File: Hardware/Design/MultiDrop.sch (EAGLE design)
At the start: 14 parts

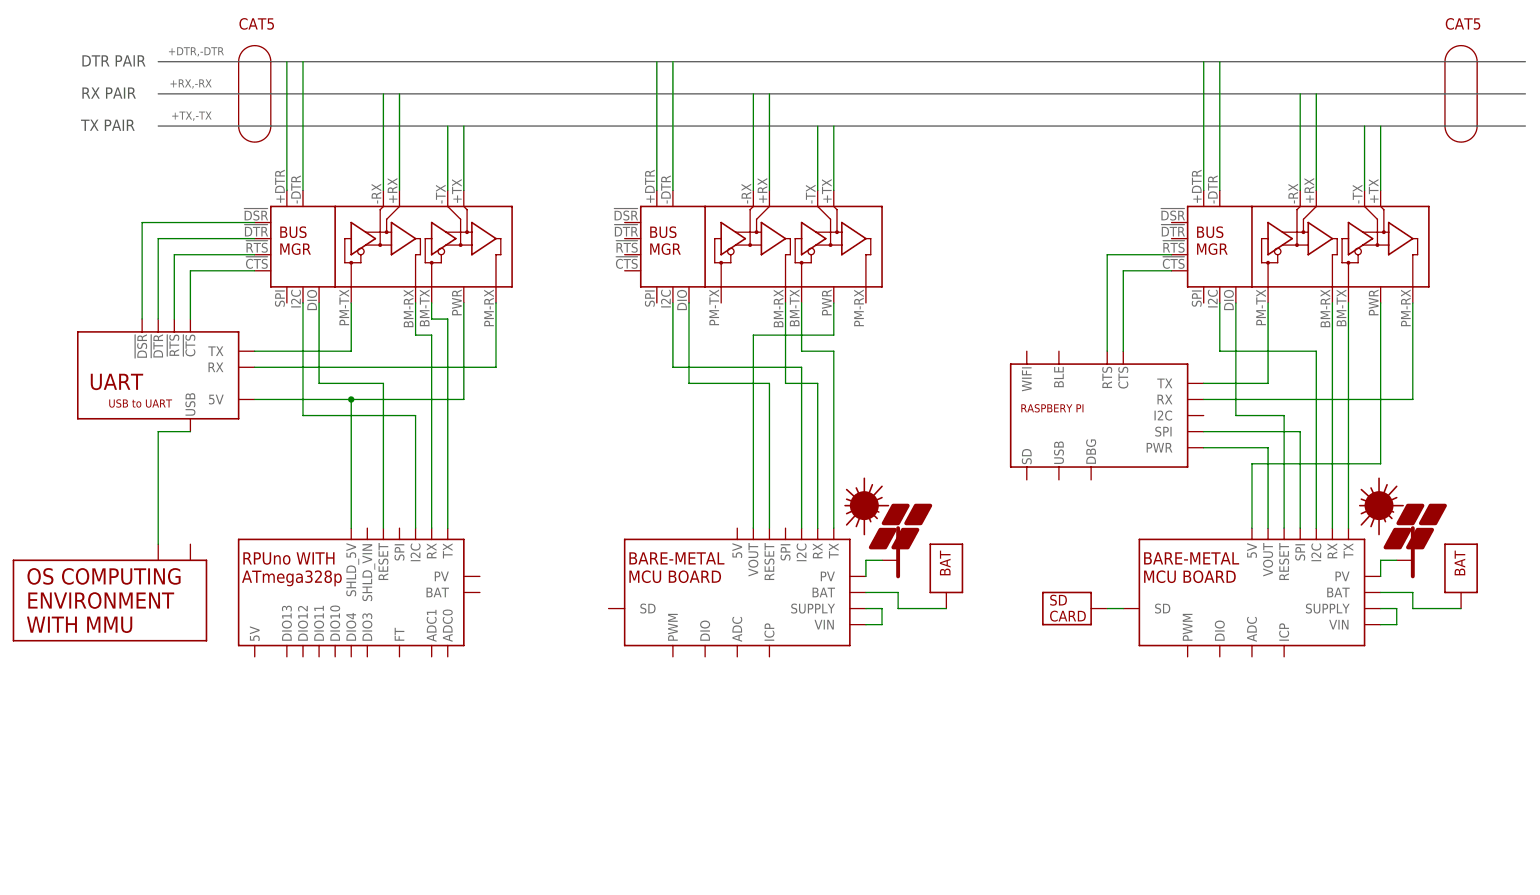
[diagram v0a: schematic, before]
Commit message: example is a little more refined
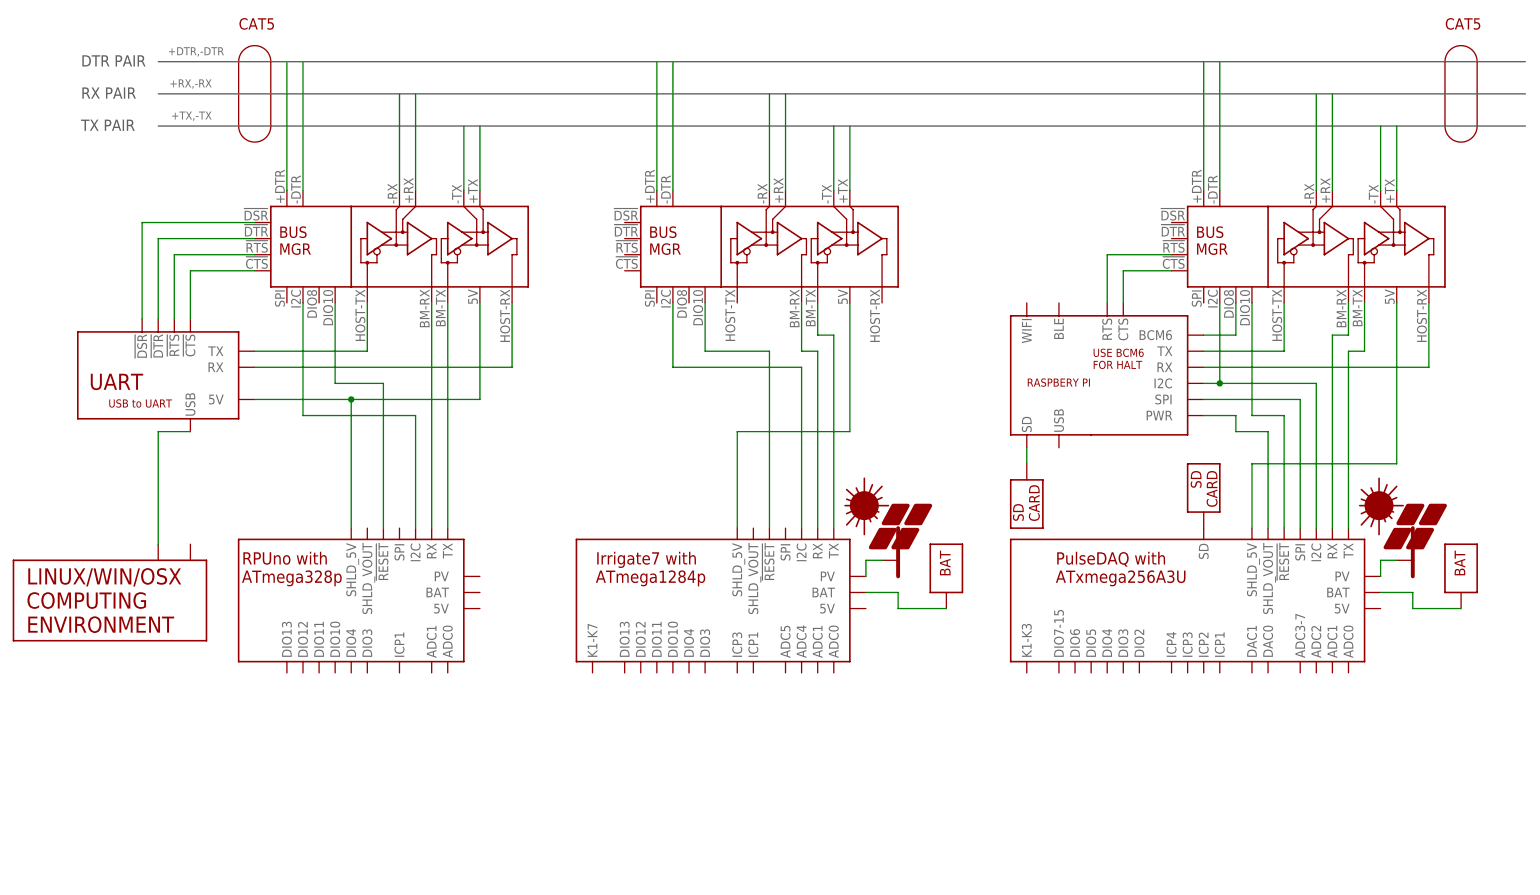
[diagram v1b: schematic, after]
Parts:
- removed BM1, BM3: (no value), Documentation:BARE-METAL
- removed PM2: (no value), Documentation:TRUSTWORTHY
- added PM1: (no value), Documentation:DESKTOP
- added SD2: SD, Documentation:SD
- added U$4: BUS_MGR, Documentation:BUS_MGR
- added U$6: PULSEDAQ, Documentation:PULSEDAQ
- U$5: value BUS_MGR -> IRRIGATE7; device Documentation:BUS_MGR -> Documentation:IRRIGATE7
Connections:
- removed net N$38: BM1.SUPPLY, BM1.VIN
- removed net N$40: BM3.SUPPLY, BM3.VIN
- removed net N$42: BM3.SD, SD3.PV_PWR
- new net N$13: U$1.PWR, U$6.SHLD_5V
- new net N$16: SD3.PV_PWR, U$6.SD
- new net N$28: SD2.PV_PWR, U$3.SD
- net +DTR: now also U$4.+DTR; no longer U$1.+DTR
- net +DTR3: now also U$1.+DTR; no longer U$5.+DTR
- net +RX: now also U$4.+RX; no longer U$1.+RX
- net +RX3: now also U$1.+RX; no longer U$5.+RX
- net +TX: now also U$4.+TX; no longer U$1.+TX
- net +TX3: now also U$1.+TX; no longer U$5.+TX
- net -DTR: now also U$4.-DTR; no longer U$1.-DTR
- net -DTR3: now also U$1.-DTR; no longer U$5.-DTR
- net -RX: now also U$4.-RX; no longer U$1.-RX
- net -RX3: now also U$1.-RX; no longer U$5.-RX
- net -TX: now also U$4.-TX; no longer U$1.-TX
- net -TX3: now also U$1.-TX; no longer U$5.-TX
- net N$1: now also U$4.BM_TX; no longer U$1.BM_TX
- net N$10: now also U$5.TX; no longer BM1.TX
- net N$11: now also U$5.RX; no longer BM1.RX
- net N$12: now also U$1.DIO8, U$3.BCM6; no longer BM3.5V, U$5.PWR
- net N$14: now also U$1.BM_TX, U$6.TX; no longer BM3.TX, U$5.BM_TX
- net N$17: now also U$5.BAT; no longer BM1.BAT
- net N$2: now also U$4.BM_RX; no longer U$1.BM_RX
- net N$21: now also U$1.BM_RX, U$6.RX; no longer BM3.RX, U$5.BM_RX
- net N$22: now also U$1.!CTS; no longer U$5.!CTS
- net N$23: now also U$1.!RTS; no longer U$5.!RTS
- net N$25: now also U$6.SPI; no longer BM3.SPI
- net N$26: now also U$1.HOST_RX; no longer U$5.PM_RX
- net N$27: now also U$1.HOST_TX; no longer U$5.PM_TX
- net N$29: now also U$4.PWR; no longer U$1.PWR
- net N$3: now also PM1.RX; no longer PM2.RX
- net N$30: now also BM2.!RESET, U$4.DIO10; no longer BM2.RESET, U$1.DIO
- net N$31: now also U$6.BAT; no longer BM3.BAT
- net N$32: now also U$1.I2C, U$3.I2C, U$6.I2C; no longer BM3.I2C, U$5.I2C
- net N$33: now also U$4.I2C; no longer U$1.I2C
- net N$34: now also U$6.PV; no longer BM3.PV
- net N$36: now also U$5.PV; no longer BM1.PV
- net N$4: now also U$4.!CTS; no longer U$1.!CTS
- net N$41: now also U$6.SHLD_VOUT; no longer BM3.VOUT
- net N$43: now also U$1.DIO10, U$6.!RESET; no longer BM3.RESET, U$5.DIO
- net N$44: now also U$2.DIO10, U$5.!RESET; no longer BM1.RESET, U$2.DIO
- net N$45: now also U$5.SHLD_5V; no longer BM1.VOUT
- net N$48: now also U$5.I2C; no longer BM1.I2C
- net N$5: now also U$4.!RTS; no longer U$1.!RTS
- net N$6: now also U$4.!DTR; no longer U$1.!DTR
- net N$7: now also U$4.!DSR; no longer U$1.!DSR
- net N$8: now also U$4.HOST_RX; no longer U$1.PM_RX
- net N$9: now also U$4.HOST_TX; no longer U$1.PM_TX
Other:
- note removed: "Irrigate7"
- note removed: "PulseDAQ"
- note removed: "RPUno"

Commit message: Hardware: example
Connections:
- net N$32: no longer U$3.I2C
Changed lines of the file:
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@@
 <wire x1="238.76" y1="93.98" x2="238.76" y2="104.14" width="0.1524" layer="94"/>
 <text x="233.68" y="109.22" size="1.778" layer="94">CAT5</text>
-<text x="165.354" y="82.296" size="5.08" layer="98">RPUpi</text>
+<text x="165.354" y="79.756" size="5.08" layer="98">RPUpi</text>
 <wire x1="15.24" y1="88.9" x2="88.9" y2="88.9" width="0.3048" layer="98" style="shortdash"/>
 <wire x1="88.9" y1="88.9" x2="88.9" y2="43.18" width="0.3048" layer="98" style="shortdash"/>
 <wire x1="88.9" y1="43.18" x2="15.24" y2="43.18" width="0.3048" layer="98" style="shortdash"/>
 <wire x1="15.24" y1="43.18" x2="15.24" y2="88.9" width="0.3048" layer="98" style="shortdash"/>
-<wire x1="93.98" y1="88.9" x2="147.32" y2="88.9" width="0.3048" layer="98" style="shortdash"/>
-<wire x1="147.32" y1="88.9" x2="147.32" y2="43.18" width="0.3048" layer="98" style="shortdash"/>
-<wire x1="147.32" y1="43.18" x2="93.98" y2="43.18" width="0.3048" layer="98" style="shortdash"/>
+<wire x1="93.98" y1="88.9" x2="149.86" y2="88.9" width="0.3048" layer="98" style="shortdash"/>
+<wire x1="149.86" y1="88.9" x2="149.86" y2="43.18" width="0.3048" layer="98" style="shortdash"/>
+<wire x1="149.86" y1="43.18" x2="93.98" y2="43.18" width="0.3048" layer="98" style="shortdash"/>
 <wire x1="93.98" y1="43.18" x2="93.98" y2="88.9" width="0.3048" layer="98" style="shortdash"/>
-<wire x1="157.48" y1="88.9" x2="157.48" y2="43.18" width="0.3048" layer="98" style="shortdash"/>
-<wire x1="157.48" y1="43.18" x2="238.76" y2="43.18" width="0.3048" layer="98" style="shortdash"/>
+<wire x1="157.48" y1="88.9" x2="157.48" y2="66.04" width="0.3048" layer="98" style="shortdash"/>
+<wire x1="157.48" y1="66.04" x2="190.5" y2="66.04" width="0.3048" layer="98" style="shortdash"/>
+<wire x1="190.5" y1="66.04" x2="190.5" y2="43.18" width="0.3048" layer="98" style="shortdash"/>
+<wire x1="190.5" y1="43.18" x2="238.76" y2="43.18" width="0.3048" layer="98" style="shortdash"/>
 <wire x1="238.76" y1="43.18" x2="238.76" y2="88.9" width="0.3048" layer="98" style="shortdash"/>
 <wire x1="238.76" y1="88.9" x2="157.48" y2="88.9" width="0.3048" layer="98" style="shortdash"/>
@@
 <instance part="PV2" gate="G$1" x="147.32" y="25.4"/>
 <instance part="PV4" gate="G$1" x="228.6" y="25.4"/>
-<instance part="SD2" gate="G$1" x="167.64" y="33.02" rot="R90"/>
+<instance part="SD2" gate="G$1" x="162.56" y="35.56" rot="R90"/>
 <instance part="U$7" gate="G$1" x="236.22" y="25.4" rot="R270"/>
 <instance part="U$9" gate="G$1" x="154.94" y="25.4" rot="R270"/>
-<instance part="SD3" gate="G$1" x="195.58" y="38.1" rot="R270"/>
+<instance part="SD3" gate="G$1" x="172.72" y="38.1" rot="R270"/>
 <instance part="BM2" gate="G$1" x="60.96" y="20.32"/>
-<instance part="U$3" gate="G$1" x="175.26" y="55.88"/>
+<instance part="U$3" gate="G$1" x="170.18" y="55.88"/>
 <instance part="U$1" gate="G$1" x="215.9" y="76.2"/>
 <instance part="U$2" gate="G$1" x="129.54" y="76.2"/>
@@
 <net name="N$22" class="0">
 <segment>
-<wire x1="190.5" y1="71.12" x2="182.88" y2="71.12" width="0.1524" layer="91"/>
-<wire x1="182.88" y1="71.12" x2="182.88" y2="66.04" width="0.1524" layer="91"/>
+<wire x1="190.5" y1="71.12" x2="177.8" y2="71.12" width="0.1524" layer="91"/>
+<wire x1="177.8" y1="71.12" x2="177.8" y2="66.04" width="0.1524" layer="91"/>
 <pinref part="U$3" gate="G$1" pin="CTS"/>
 <pinref part="U$1" gate="G$1" pin="!CTS"/>
@@
 <net name="N$23" class="0">
 <segment>
-<wire x1="180.34" y1="66.04" x2="180.34" y2="73.66" width="0.1524" layer="91"/>
-<wire x1="180.34" y1="73.66" x2="190.5" y2="73.66" width="0.1524" layer="91"/>
+<wire x1="175.26" y1="66.04" x2="175.26" y2="73.66" width="0.1524" layer="91"/>
+<wire x1="175.26" y1="73.66" x2="190.5" y2="73.66" width="0.1524" layer="91"/>
 <pinref part="U$3" gate="G$1" pin="RTS"/>
 <pinref part="U$1" gate="G$1" pin="!RTS"/>
@@
 <segment>
 <wire x1="231.14" y1="55.88" x2="231.14" y2="66.04" width="0.1524" layer="91"/>
-<wire x1="195.58" y1="55.88" x2="231.14" y2="55.88" width="0.1524" layer="91"/>
+<wire x1="190.5" y1="55.88" x2="231.14" y2="55.88" width="0.1524" layer="91"/>
 <pinref part="U$3" gate="G$1" pin="RX"/>
 <pinref part="U$1" gate="G$1" pin="HOST_RX"/>
@@
 <segment>
 <wire x1="208.28" y1="58.42" x2="208.28" y2="66.04" width="0.1524" layer="91"/>
-<wire x1="195.58" y1="58.42" x2="208.28" y2="58.42" width="0.1524" layer="91"/>
+<wire x1="190.5" y1="58.42" x2="208.28" y2="58.42" width="0.1524" layer="91"/>
 <pinref part="U$3" gate="G$1" pin="TX"/>
 <pinref part="U$1" gate="G$1" pin="HOST_TX"/>
@@
 <wire x1="213.36" y1="53.34" x2="198.12" y2="53.34" width="0.1524" layer="91"/>
 <wire x1="198.12" y1="53.34" x2="198.12" y2="66.04" width="0.1524" layer="91"/>
-<wire x1="195.58" y1="53.34" x2="198.12" y2="53.34" width="0.1524" layer="91"/>
-<junction x="198.12" y="53.34"/>
-<pinref part="U$3" gate="G$1" pin="I2C"/>
 <pinref part="U$1" gate="G$1" pin="I2C"/>
 <pinref part="U$6" gate="G$1" pin="I2C"/>
@@
 <net name="N$25" class="0">
 <segment>
-<wire x1="195.58" y1="50.8" x2="210.82" y2="50.8" width="0.1524" layer="91"/>
+<wire x1="190.5" y1="50.8" x2="210.82" y2="50.8" width="0.1524" layer="91"/>
 <wire x1="210.82" y1="50.8" x2="210.82" y2="30.48" width="0.1524" layer="91"/>
 <pinref part="U$3" gate="G$1" pin="SPI"/>
@@
 <pinref part="SD2" gate="G$1" pin="PV_PWR"/>
 <pinref part="U$3" gate="G$1" pin="SD"/>
-<wire x1="167.64" y1="40.64" x2="167.64" y2="43.18" width="0.1524" layer="91"/>
 </segment>
 </net>
@@
 <pinref part="U$3" gate="G$1" pin="PWR"/>
 <pinref part="U$6" gate="G$1" pin="SHLD_VOUT"/>
-<wire x1="200.66" y1="48.26" x2="195.58" y2="48.26" width="0.1524" layer="91"/>
+<wire x1="190.5" y1="48.26" x2="200.66" y2="48.26" width="0.1524" layer="91"/>
 <wire x1="200.66" y1="48.26" x2="200.66" y2="45.72" width="0.1524" layer="91"/>
 <wire x1="200.66" y1="45.72" x2="205.74" y2="45.72" width="0.1524" layer="91"/>
@@
 <segment>
 <pinref part="U$3" gate="G$1" pin="BCM6"/>
-<wire x1="195.58" y1="60.96" x2="200.66" y2="60.96" width="0.1524" layer="91"/>
+<wire x1="190.5" y1="60.96" x2="200.66" y2="60.96" width="0.1524" layer="91"/>
 <pinref part="U$1" gate="G$1" pin="DIO8"/>
 <wire x1="200.66" y1="60.96" x2="200.66" y2="66.04" width="0.1524" layer="91"/>

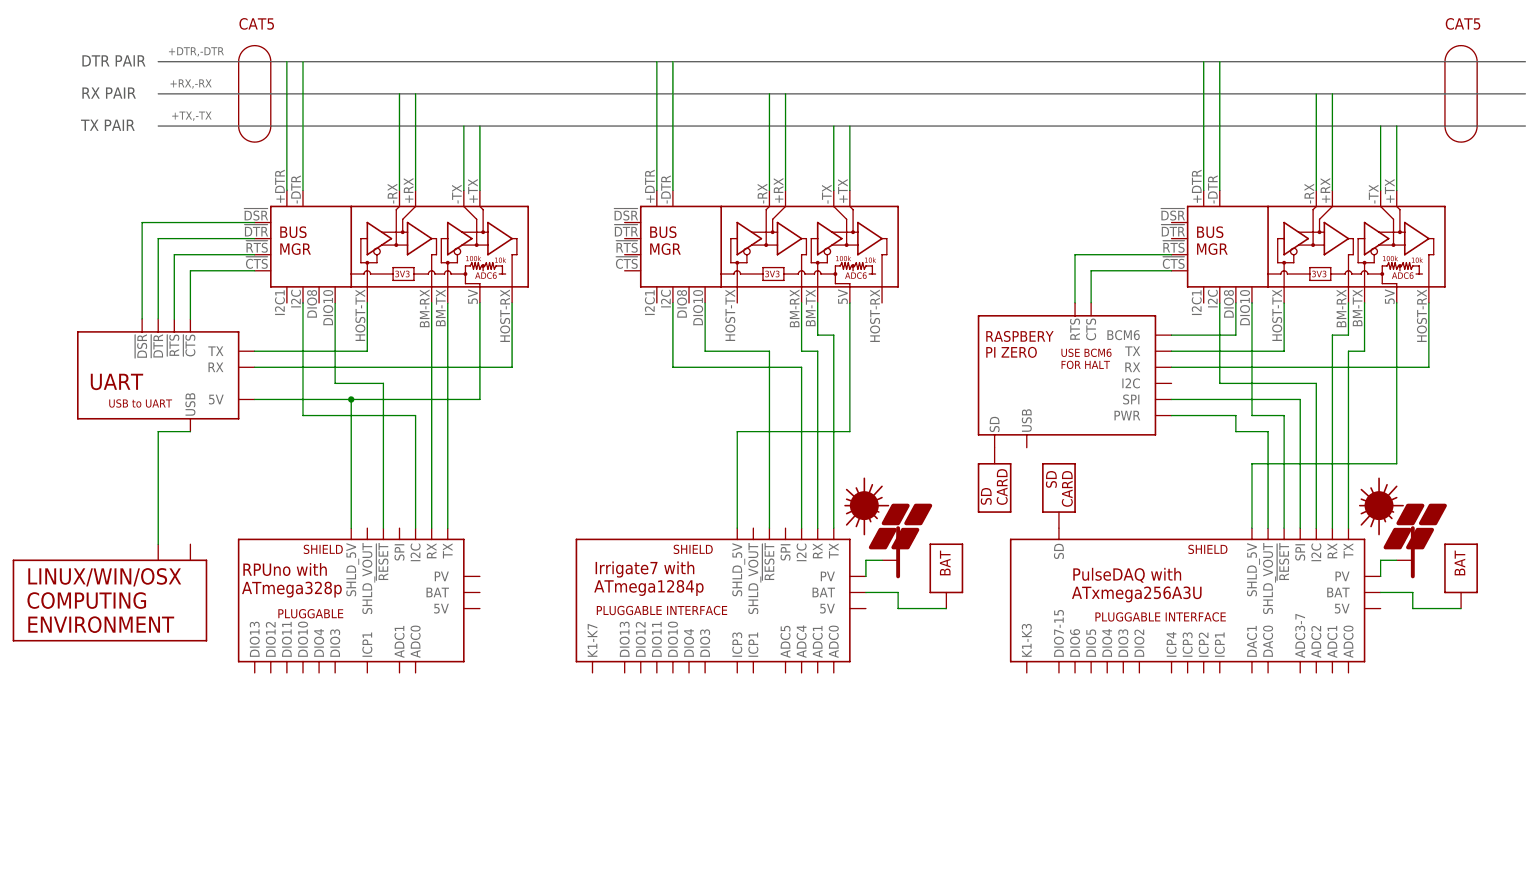
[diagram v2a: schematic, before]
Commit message: Hardware: update multidrop example
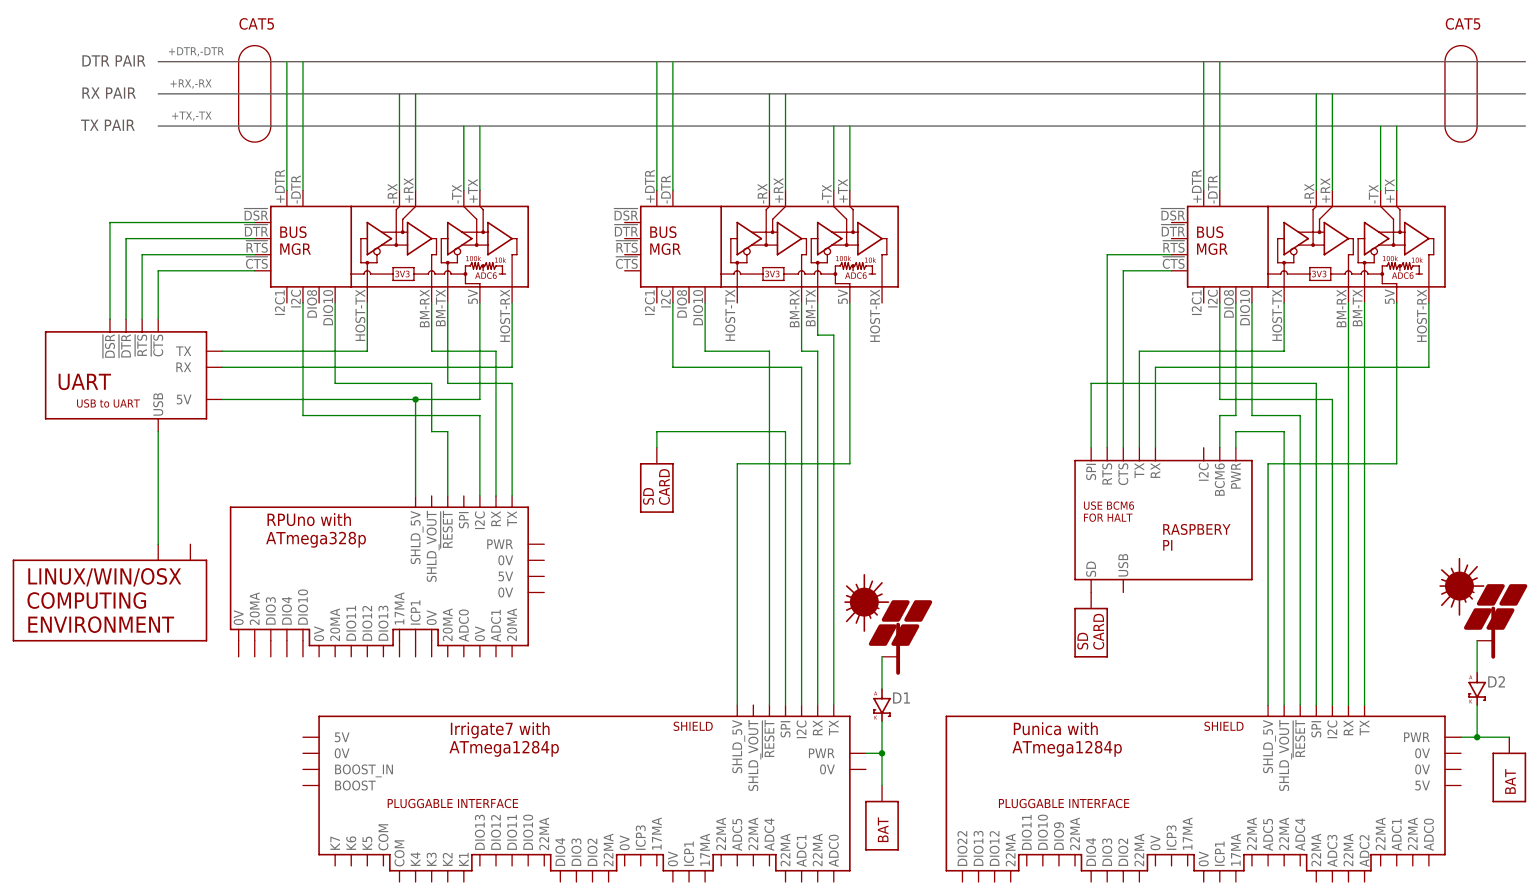
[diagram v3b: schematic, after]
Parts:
- removed SD3: SD, Documentation:SD
- removed U$6: PULSEDAQ, Documentation:PULSEDAQ
- added D1, D2: (no value), D-SBR:DSMB
- added SD1: SD, Documentation:SD
- added U$8: PUNICA, Documentation:PUNICA
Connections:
- removed net N$31: U$6.BAT, U$7.BAT_PWR
- removed net N$34: PV4.PV_PWR, U$6.PV
- removed net N$36: PV2.PV_PWR, U$5.PV
- new net N$15: D2.K, U$7.BAT_PWR, U$8.PWR
- new net N$18: D1.K, U$5.PWR, U$9.BAT_PWR
- new net N$19: SD1.PV_PWR, U$5.SPI
- net N$13: now also U$8.SHLD_5V; no longer U$6.SHLD_5V
- net N$14: now also U$8.TX; no longer U$6.TX
- net N$16: now also D2.A, PV4.PV_PWR; no longer SD3.PV_PWR, U$6.SD
- net N$17: now also D1.A, PV2.PV_PWR; no longer U$5.BAT, U$9.BAT_PWR
- net N$21: now also U$8.RX; no longer U$6.RX
- net N$25: now also U$8.SPI; no longer U$6.SPI
- net N$32: now also U$8.I2C; no longer U$6.I2C
- net N$41: now also U$8.SHLD_VOUT; no longer U$6.SHLD_VOUT
- net N$43: now also U$8.!RESET; no longer U$6.!RESET
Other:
- note added: "IOFF"
